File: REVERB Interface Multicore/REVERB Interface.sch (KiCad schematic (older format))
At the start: 65 parts, among them J1 RPiZeroW, J2 Iridium, J3 APRS, J4 Antenna, J5 UPDI, J6 USBPWR, M1 MountingHole_Pad, M2 MountingHole_Pad, M3 MountingHole_Pad, M4 MountingHole_Pad, M5 PiMount, M6 PiMount, M7 PiMount, M8 PiMount, U1 IMU, U2 MAX3232, U3 ATtiny1604-SS, U4 TXB0104D, U5 DS3232M

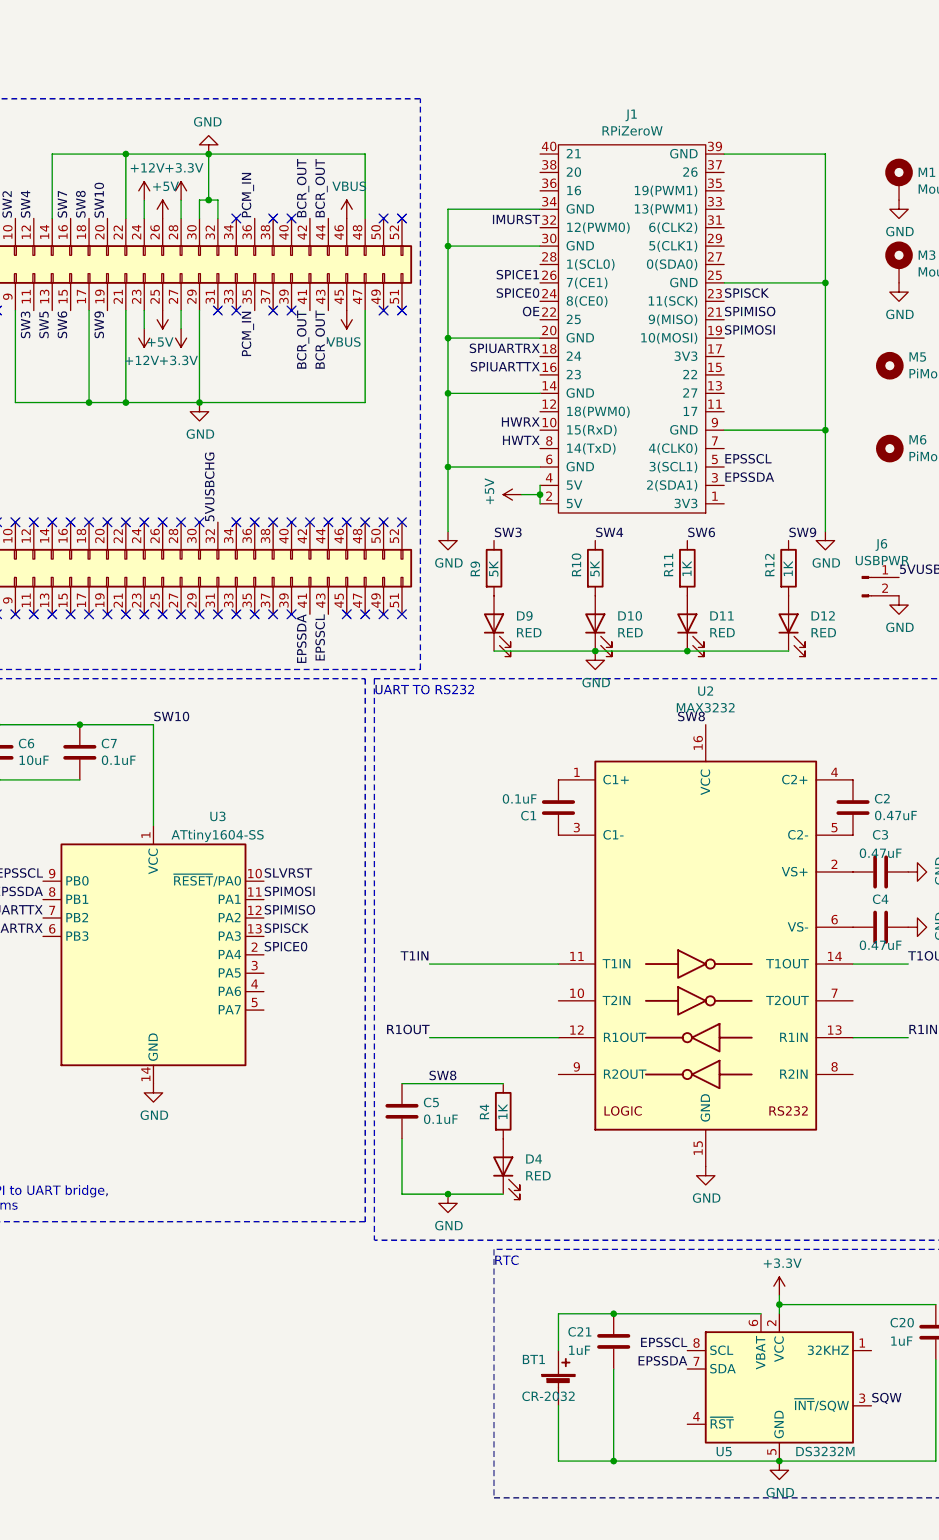
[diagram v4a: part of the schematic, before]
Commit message: add i2c0 option
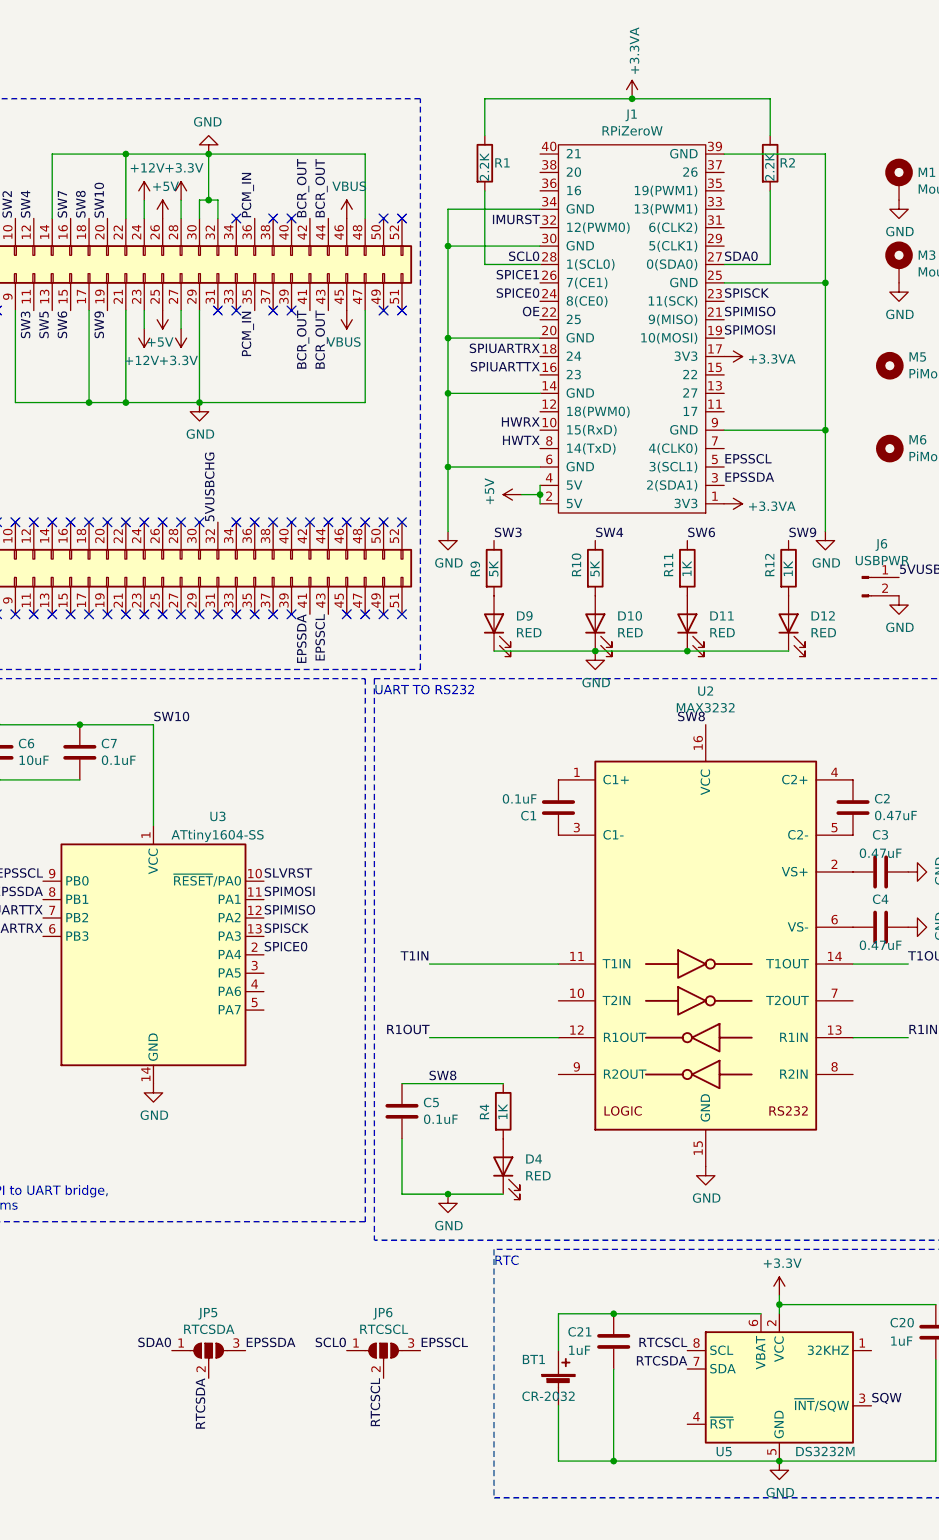
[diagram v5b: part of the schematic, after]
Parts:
- added JP5: RTCSDA, Jumper:SolderJumper-3_P1.3mm_Open_Pad1.0x1.5mm_NumberLabels, symbol Jumper:SolderJumper_3_Open
- added JP6: RTCSCL, Jumper:SolderJumper-3_P1.3mm_Open_Pad1.0x1.5mm_NumberLabels, symbol Jumper:SolderJumper_3_Open
- added R1, R2: 2.2K, Resistor_SMD:R_1206_3216Metric_Pad1.30x1.75mm_HandSolder, symbol Device:R
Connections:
- net EPSSCL: now also JP6.3 (B); no longer U5.8 (SCL)
- net EPSSDA: now also JP5.3 (B); no longer U5.7 (SDA)
- net +3.3VA: now reaches J1.1 (3V3)
- net +3.3VA: now also J1.17 (3V3), R1.1, R2.1
- net SDA0: now reaches J1.27 (0(SDA0))
- net SDA0: now also JP5.1 (A), R2.2
- net SCL0: now reaches J1.28 (1(SCL0))
- net SCL0: now also JP6.1 (A), R1.2
- new net RTCSCL: JP6.2 (C), U5.8 (SCL)
- new net RTCSDA: JP5.2 (C), U5.7 (SDA)
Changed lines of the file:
@@
 	1    0    0    -1
 $EndComp
-Text Label 5400 7300 2    50   ~ 0
+Text Label 3950 7300 0    50   ~ 0
 EPSSCL
-Text Label 5400 7400 2    50   ~ 0
+Text Label 3000 7300 0    50   ~ 0
 EPSSDA
 $Comp
@@
 Wire Wire Line
 	4000 5600 4700 5600
+$Comp
+L power:+3.3VA #PWR010
+U 1 1 61A144F2
+P 5600 2700
+F 0 "#PWR010" H 5600 2550 50  0001 C CNN
+F 1 "+3.3VA" V 5615 2828 50  0000 L CNN
+F 2 "" H 5600 2700 50  0001 C CNN
+F 3 "" H 5600 2700 50  0001 C CNN
+	1    5600 2700
+	0    1    1    0
+$EndComp
+$Comp
+L power:+3.3VA #PWR09
+U 1 1 61A1537F
+P 5600 1900
+F 0 "#PWR09" H 5600 1750 50  0001 C CNN
+F 1 "+3.3VA" V 5615 2028 50  0000 L CNN
+F 2 "" H 5600 1900 50  0001 C CNN
+F 3 "" H 5600 1900 50  0001 C CNN
+	1    5600 1900
+	0    1    1    0
+$EndComp
+$Comp
+L power:+3.3VA #PWR05
+U 1 1 61A1C1E9
+P 5100 500
+F 0 "#PWR05" H 5100 350 50  0001 C CNN
+F 1 "+3.3VA" V 5115 628 50  0000 L CNN
+F 2 "" H 5100 500 50  0001 C CNN
+F 3 "" H 5100 500 50  0001 C CNN
+	1    5100 500
+	1    0    0    -1
+$EndComp
+$Comp
+L Device:R R2
+U 1 1 61A20648
+P 5850 850
+F 0 "R2" H 5900 850 50  0000 L CNN
+F 1 "2.2K" V 5850 750 50  0000 L CNN
+F 2 "Resistor_SMD:R_1206_3216Metric_Pad1.30x1.75mm_HandSolder" V 5780 850 50  0001 C CNN
+F 3 "~" H 5850 850 50  0001 C CNN
+	1    5850 850
+	1    0    0    -1
+$EndComp
+Text Label 5600 1400 0    50   ~ 0
+SDA0
+Text Label 4600 1400 2    50   ~ 0
+SCL0
+Wire Wire Line
+	5600 1400 5850 1400
+Wire Wire Line
+	5850 1400 5850 1000
+$Comp
+L Device:R R1
+U 1 1 61A29CEA
+P 4300 850
+F 0 "R1" H 4350 850 50  0000 L CNN
+F 1 "2.2K" V 4300 750 50  0000 L CNN
+F 2 "Resistor_SMD:R_1206_3216Metric_Pad1.30x1.75mm_HandSolder" V 4230 850 50  0001 C CNN
+F 3 "~" H 4300 850 50  0001 C CNN
+	1    4300 850
+	1    0    0    -1
+$EndComp
+Wire Wire Line
+	5850 700  5850 500
+Wire Wire Line
+	5850 500  5100 500
+Wire Wire Line
+	5100 500  4300 500
+Wire Wire Line
+	4300 500  4300 700
+Connection ~ 5100 500
+Wire Wire Line
+	4300 1000 4300 1400
+Wire Wire Line
+	4300 1400 4600 1400
+$Comp
+L Jumper:SolderJumper_3_Open JP6
+U 1 1 61A39415
+P 3750 7300
+F 0 "JP6" H 3750 7505 50  0000 C CNN
+F 1 "RTCSCL" H 3750 7414 50  0000 C CNN
+F 2 "Jumper:SolderJumper-3_P1.3mm_Open_Pad1.0x1.5mm_NumberLabels" H 3750 7300 50  0001 C CNN
+F 3 "~" H 3750 7300 50  0001 C CNN
+	1    3750 7300
+	1    0    0    -1
+$EndComp
+$Comp
+L Jumper:SolderJumper_3_Open JP5
+U 1 1 61A3B0DA
+P 2800 7300
+F 0 "JP5" H 2800 7505 50  0000 C CNN
+F 1 "RTCSDA" H 2800 7414 50  0000 C CNN
+F 2 "Jumper:SolderJumper-3_P1.3mm_Open_Pad1.0x1.5mm_NumberLabels" H 2800 7300 50  0001 C CNN
+F 3 "~" H 2800 7300 50  0001 C CNN
+	1    2800 7300
+	1    0    0    -1
+$EndComp
+Text Label 5400 7300 2    50   ~ 0
+RTCSCL
+Text Label 5400 7400 2    50   ~ 0
+RTCSDA
+Text Label 3750 7450 3    50   ~ 0
+RTCSCL
+Text Label 2800 7450 3    50   ~ 0
+RTCSDA
+Text Label 3550 7300 2    50   ~ 0
+SCL0
+Text Label 2600 7300 2    50   ~ 0
+SDA0
 $EndSCHEMATC

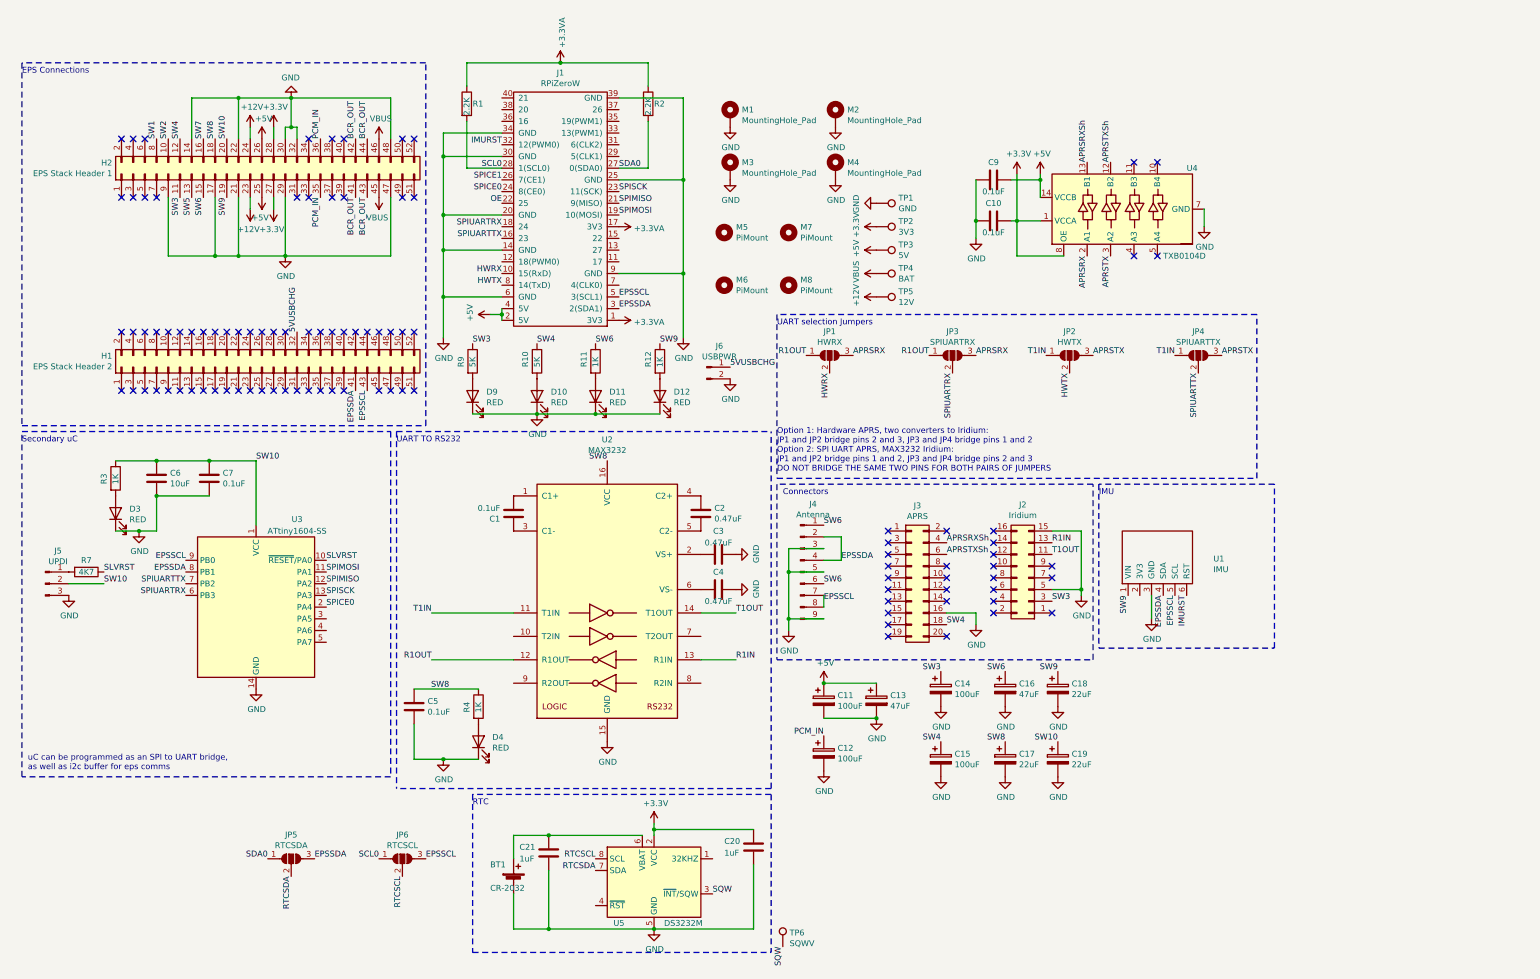
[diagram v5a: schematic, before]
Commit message: finish tidying up schematics
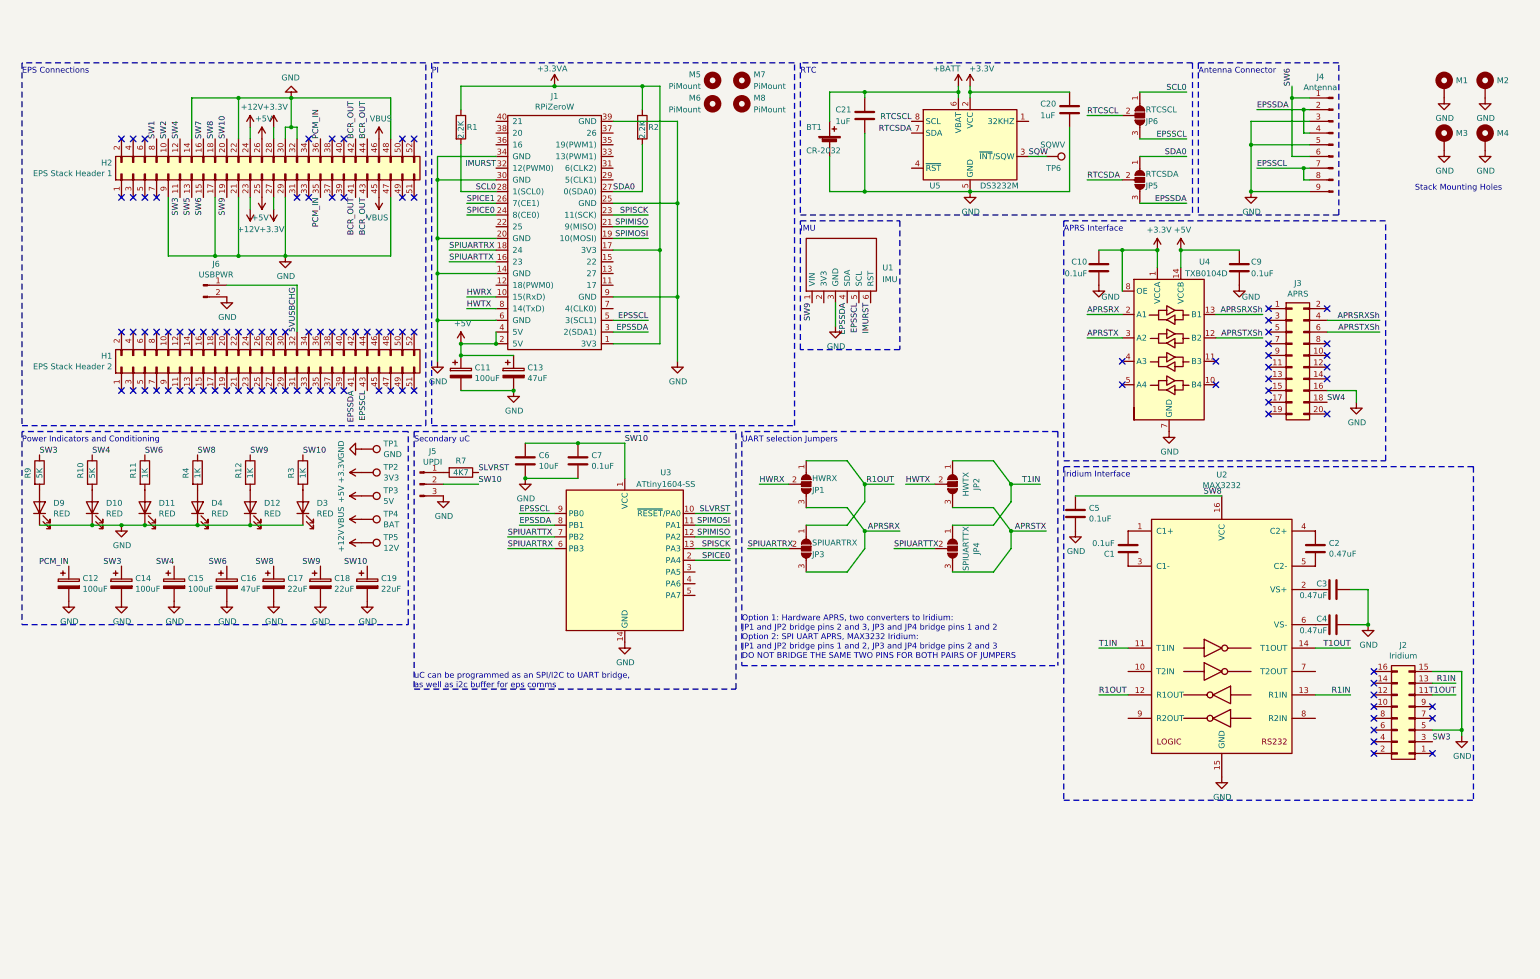
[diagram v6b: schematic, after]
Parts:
- M1, M2, M3, M4: value MountingHole_Pad -> Stack Mounting Hole
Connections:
- net +BATT: now reaches BT1.1 (+), C21.1, U5.6 (VBAT)
- net OE: no longer names the net of J1.22 (25)
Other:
- note added: "APRS Interface"
- note added: "Antenna Connector"
- note added: "Iridium Interface"
- note added: "PI"
- note added: "Power Indicators and Conditioning"
- note added: "Stack Mounting Holes"
- note added: "uC can be programmed as an SPI/I2C to UART bridge, \nas well as i2c buffer for eps comms"
- note removed: "Connectors"
- note removed: "UART TO RS232"
- note removed: "uC can be programmed as an SPI to UART bridge, \nas well as i2c buffer for eps comms"
- moved on the sheet: BT1, C1, C10, C11, C12, C13, C14, C15, C16, C17, C18, C19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

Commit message: new gerber exports
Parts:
- C13, C16: value 47uF -> 22uF
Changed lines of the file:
@@
 P 4700 3150
 F 0 "C13" H 4818 3196 50  0000 L CNN
-F 1 "47uF" H 4818 3105 50  0000 L CNN
+F 1 "22uF" H 4818 3105 50  0000 L CNN
 F 2 "Capacitor_Tantalum_SMD:CP_EIA-6032-28_Kemet-C_Pad2.25x2.35mm_HandSolder" H 4738 3000 50  0001 C CNN
 F 3 "~" H 4700 3150 50  0001 C CNN
@@
 P 2250 4950
 F 0 "C16" H 2368 4996 50  0000 L CNN
-F 1 "47uF" H 2368 4905 50  0000 L CNN
+F 1 "22uF" H 2368 4905 50  0000 L CNN
 F 2 "Capacitor_Tantalum_SMD:CP_EIA-6032-28_Kemet-C_Pad2.25x2.35mm_HandSolder" H 2288 4800 50  0001 C CNN
 F 3 "~" H 2250 4950 50  0001 C CNN
